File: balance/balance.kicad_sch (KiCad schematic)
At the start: 8 parts, among them M1 Motor_DC, M2 Motor_DC, SW1 SW_SPST, U1 ZC142200, U2 L298N, U3 MPU-6050

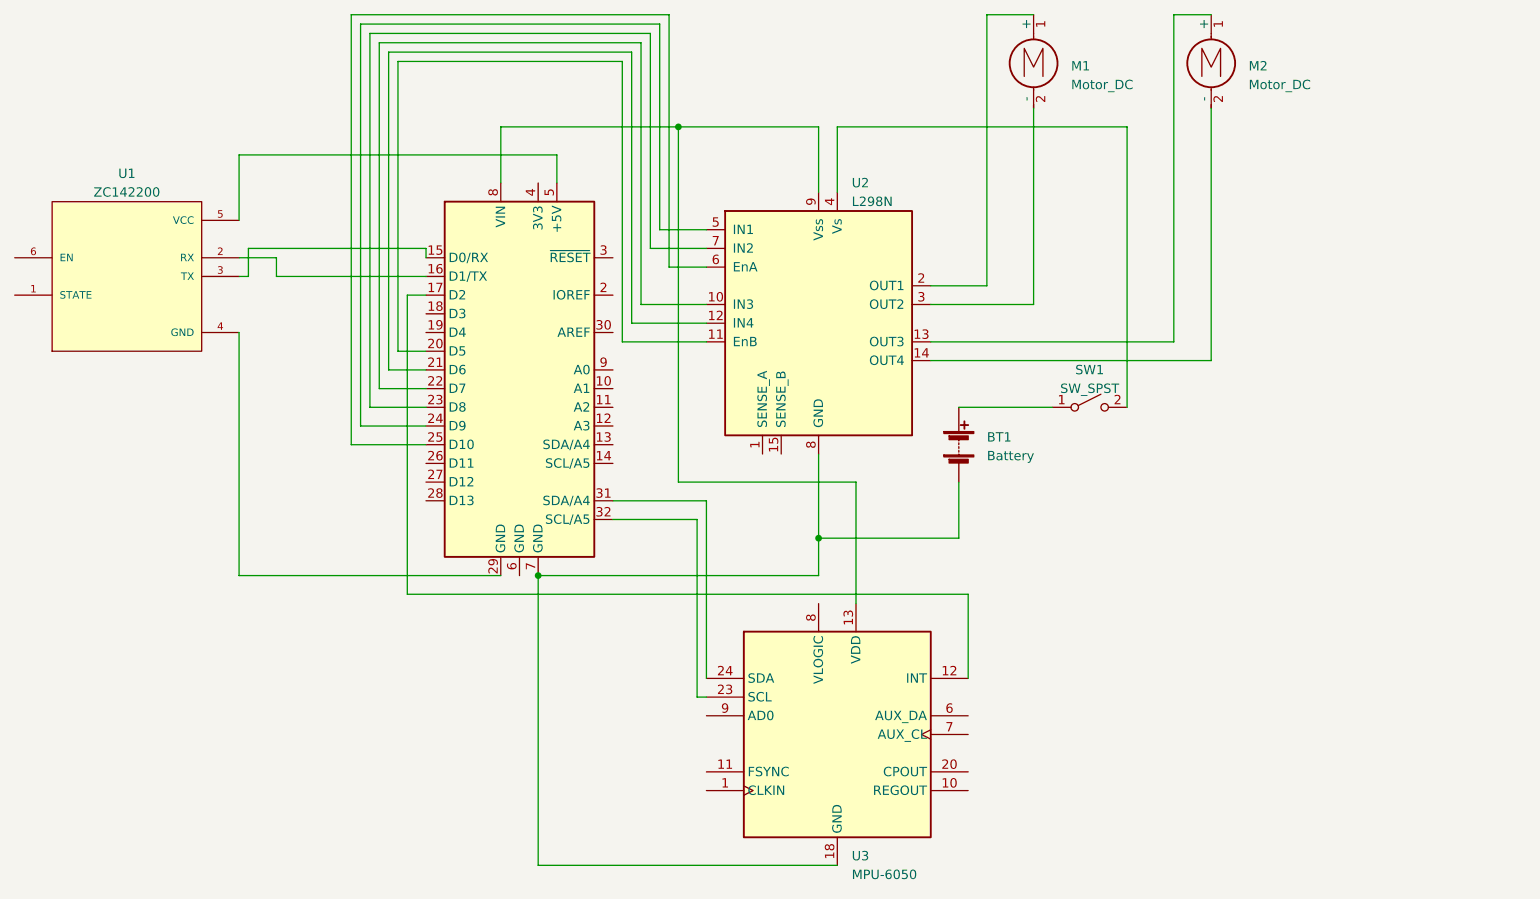
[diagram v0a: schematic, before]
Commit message: works for esp32
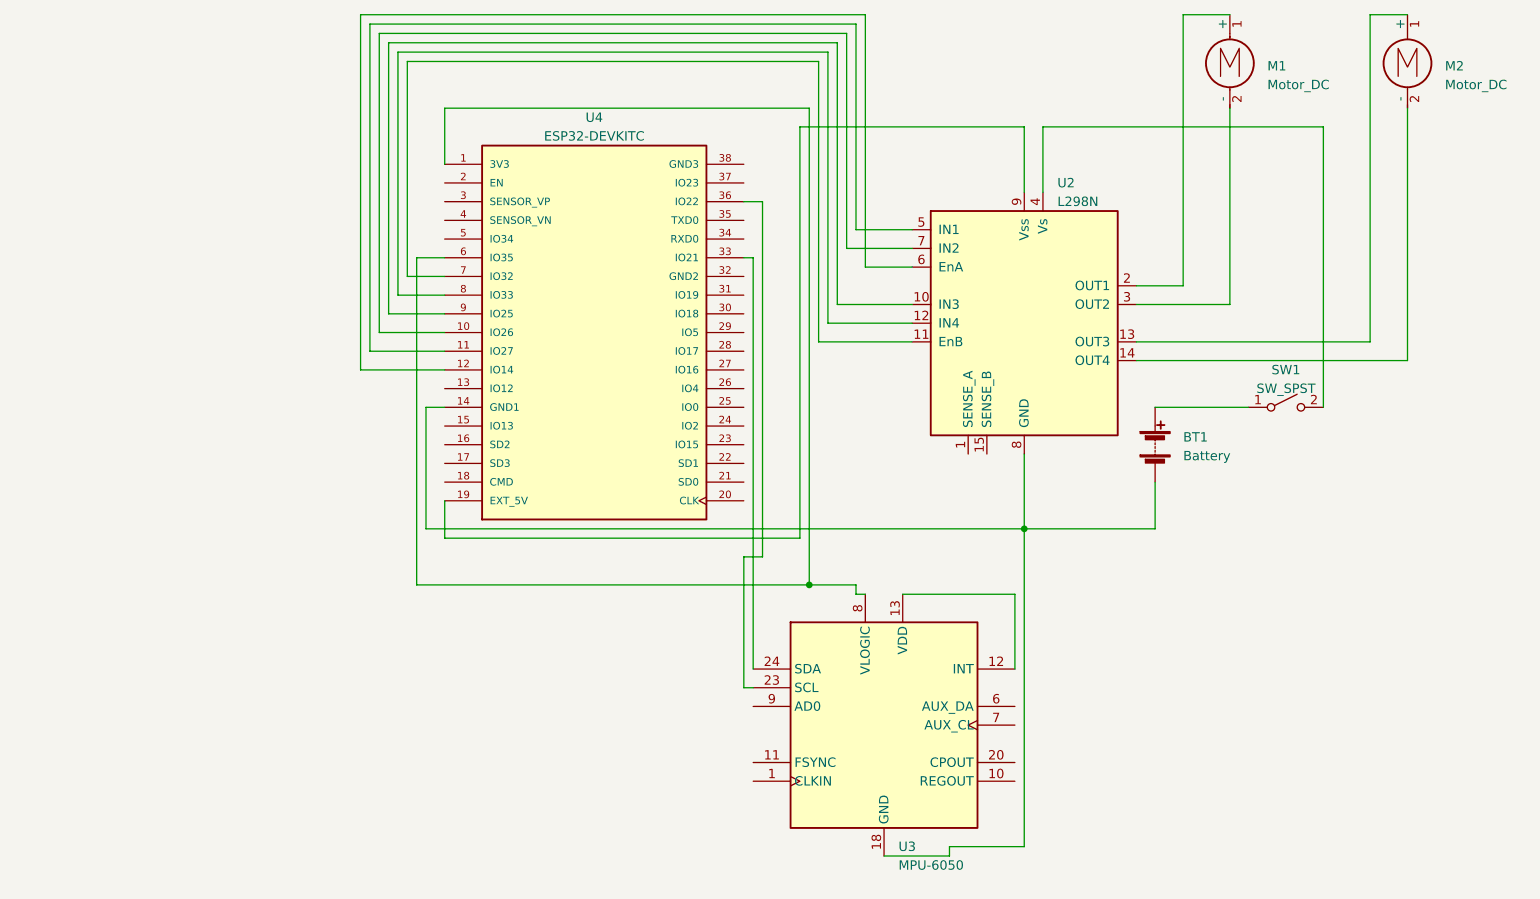
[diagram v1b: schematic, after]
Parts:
- removed A1: Arduino_UNO_R3, Module:Arduino_UNO_R3, symbol MCU_Module:Arduino_UNO_R3
- removed U1: ZC142200, MODULE_ZC142200, symbol HC-05:ZC142200
- added U4: ESP32-DEVKITC, MODULE_ESP32-DEVKITC, symbol ESP32-DEVKITC:ESP32-DEVKITC
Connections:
- net at U2.10 (IN3): now also U4.9 (IO25)
- net at U2.11 (EnB): now also U4.7 (IO32)
- net at U2.12 (IN4): now also U4.8 (IO33)
- net at U2.5 (IN1): now also U4.11 (IO27)
- net at U2.6 (EnA): now also U4.12 (IO14)
- net at U2.7 (IN2): now also U4.10 (IO26)
- net at BT1.2 (-), U2.8 (GND), U3.18 (GND): now also U4.14 (GND1)
- net at U2.9 (Vss): now also U4.19 (EXT_5V); no longer U3.13 (VDD)
- net at U3.12 (INT): now also U3.13 (VDD)
- net at U3.23 (SCL): now also U4.36 (IO22)
- net at U3.24 (SDA): now also U4.33 (IO21)
- net at U3.8 (VLOGIC): now also U4.1 (3V3), U4.6 (IO35)
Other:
- moved on the sheet: BT1, M1, M2, SW1, U2, U3

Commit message: frame done
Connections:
- net at U3.12 (INT): now also U4.6 (IO35); no longer U3.13 (VDD)
- new net: U3.13 (VDD), U4.1 (3V3)
- now unconnected: U3.8 (VLOGIC)
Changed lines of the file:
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@@
   (junction (at 184.15 111.76) (diameter 0) (color 0 0 0 0)
   )
-  (junction (at 154.94 119.38) (diameter 0) (color 0 0 0 0)
-  )
   (wire (pts (xy 161.29 43.18) (xy 95.25 43.18))
     (stroke (width 0) (type default))
@@
     (stroke (width 0) (type default))
   )
-  (wire (pts (xy 161.29 119.38) (xy 154.94 119.38))
-    (stroke (width 0) (type default))
-  )
   (wire (pts (xy 168.91 83.82) (xy 157.48 83.82))
     (stroke (width 0) (type default))
@@
     (stroke (width 0) (type default))
   )
+  (wire (pts (xy 167.64 118.11) (xy 167.64 120.65))
+    (stroke (width 0) (type default))
+  )
   (wire (pts (xy 199.39 86.36) (xy 231.14 86.36))
     (stroke (width 0) (type default))
   )
+  (wire (pts (xy 101.6 119.38) (xy 182.88 119.38))
+    (stroke (width 0) (type default))
+  )
   (wire (pts (xy 184.15 111.76) (xy 201.93 111.76))
     (stroke (width 0) (type default))
@@
     (stroke (width 0) (type default))
   )
+  (wire (pts (xy 154.94 54.61) (xy 154.94 118.11))
+    (stroke (width 0) (type default))
+  )
   (wire (pts (xy 153.67 57.15) (xy 184.15 57.15))
     (stroke (width 0) (type default))
@@
     (stroke (width 0) (type default))
   )
+  (wire (pts (xy 154.94 118.11) (xy 167.64 118.11))
+    (stroke (width 0) (type default))
+  )
   (wire (pts (xy 148.59 115.57) (xy 148.59 67.31))
     (stroke (width 0) (type default))
@@
     (stroke (width 0) (type default))
   )
-  (wire (pts (xy 154.94 54.61) (xy 154.94 119.38))
-    (stroke (width 0) (type default))
-  )
   (wire (pts (xy 158.75 81.28) (xy 158.75 45.72))
     (stroke (width 0) (type default))
@@
     (stroke (width 0) (type default))
   )
-  (wire (pts (xy 162.56 120.65) (xy 161.29 120.65))
-    (stroke (width 0) (type default))
-  )
   (wire (pts (xy 153.67 57.15) (xy 153.67 113.03))
     (stroke (width 0) (type default))
   )
-  (wire (pts (xy 182.88 130.81) (xy 182.88 120.65))
+  (wire (pts (xy 182.88 119.38) (xy 182.88 130.81))
     (stroke (width 0) (type default))
   )
@@
     (stroke (width 0) (type default))
   )
-  (wire (pts (xy 161.29 120.65) (xy 161.29 119.38))
-    (stroke (width 0) (type default))
-  )
   (wire (pts (xy 158.75 45.72) (xy 97.79 45.72))
     (stroke (width 0) (type default))
@@
     (stroke (width 0) (type default))
   )
-  (wire (pts (xy 154.94 119.38) (xy 101.6 119.38))
-    (stroke (width 0) (type default))
-  )
   (wire (pts (xy 199.39 81.28) (xy 212.09 81.28))
     (stroke (width 0) (type default))
@@
     (stroke (width 0) (type default))
   )
-  (wire (pts (xy 182.88 120.65) (xy 167.64 120.65))
-    (stroke (width 0) (type default))
-  )
